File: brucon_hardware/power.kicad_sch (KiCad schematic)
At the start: 21 parts, among them J201 WTB01W03BB, Q1 AO3400A, U1 IP5305, U203 HT75xx-1-SOT89

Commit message: Small changes
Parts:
- R1: LCSC C22977 -> C270630
- R2: LCSC C25804 -> C25744
- R203, R204: LCSC C21189 -> C17168
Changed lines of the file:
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@@
 			)
 		)
-		(property "LCSC" "C21189"
+		(property "LCSC" " C17168"
 			(at 83.82 74.93 0)
 			(effects
@@
 			)
 		)
-		(property "LCSC" "C22977"
+		(property "LCSC" "C270630"
 			(at 52.07 69.85 0)
 			(effects
@@
 			)
 		)
-		(property "LCSC" "C25804"
+		(property "LCSC" "C25744"
 			(at 111.76 91.44 0)
 			(effects
@@
 			)
 		)
-		(property "LCSC" "C21189"
+		(property "LCSC" " C17168"
 			(at 76.2 69.85 0)
 			(effects

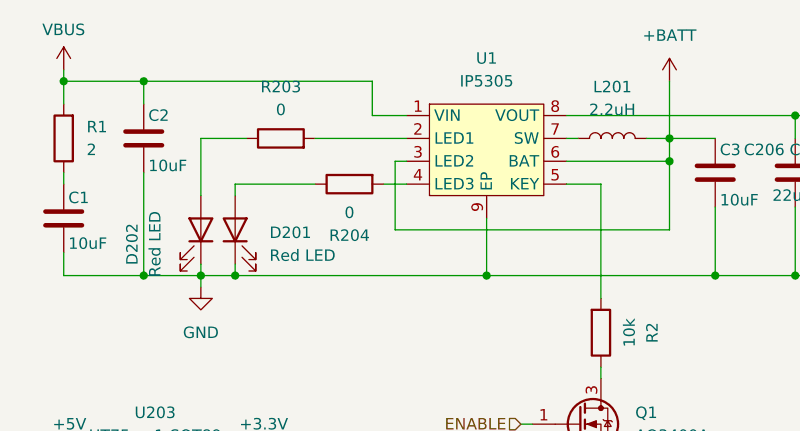
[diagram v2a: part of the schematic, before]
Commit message: Swapped IP5305 for IP5305T (needs current limiting resistors on LEDs), swapped buffer for Nexperia alternative for availability and price. Ordered 2nd prototype.
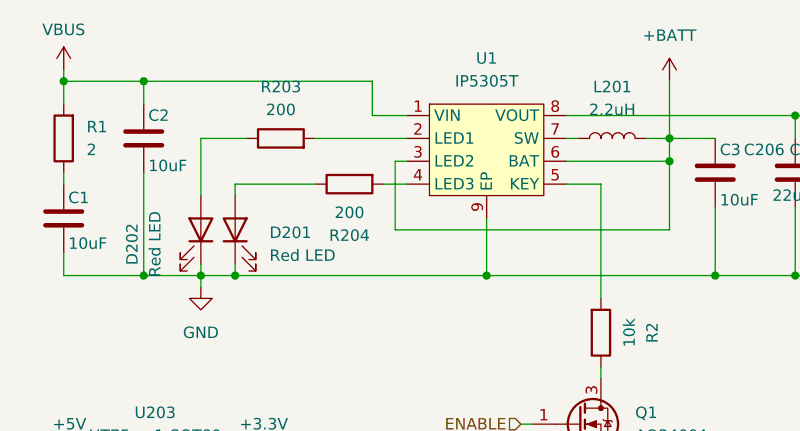
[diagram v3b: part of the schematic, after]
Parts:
- R203, R204: value 0 -> 200; LCSC C17168 -> C25087
- U1: value IP5305 -> IP5305T; LCSC C181686 -> C2982924
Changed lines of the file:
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@@
 			)
 		)
-		(property "Value" "0"
+		(property "Value" "200"
 			(at 83.82 78.105 90)
 			(effects
@@
 			)
 		)
-		(property "LCSC" " C17168"
+		(property "LCSC" "C25087"
 			(at 83.82 74.93 0)
 			(effects
@@
 			)
 		)
-		(property "Value" "IP5305"
+		(property "Value" "IP5305T"
 			(at 99.06 63.5 0)
 			(effects
@@
 			)
 		)
-		(property "Datasheet" "https://www.lcsc.com/datasheet/lcsc_datasheet_1810151710_INJOINIC-IP5305_C181686.pdf"
+		(property "Datasheet" "https://www.lcsc.com/datasheet/lcsc_datasheet_2311011131_INJOINIC-IP5305T_C2982924.pdf"
 			(at 96.52 68.58 0)
 			(effects
@@
 			)
 		)
-		(property "LCSC" "C181686"
+		(property "LCSC" "C2982924"
 			(at 99.06 69.85 0)
 			(effects
@@
 			)
 		)
-		(property "Value" "0"
+		(property "Value" "200"
 			(at 76.2 66.675 90)
 			(effects
@@
 			)
 		)
-		(property "LCSC" " C17168"
+		(property "LCSC" "C25087"
 			(at 76.2 69.85 0)
 			(effects

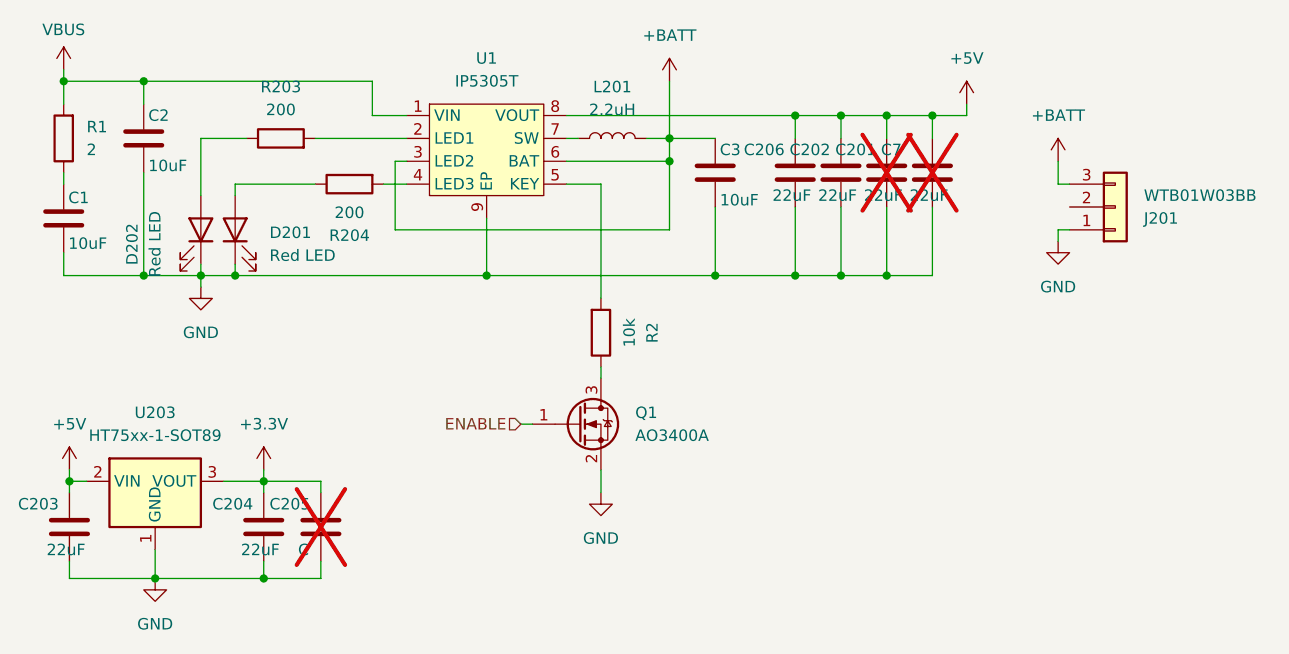
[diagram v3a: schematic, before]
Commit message: Committing final hardware as has been produced
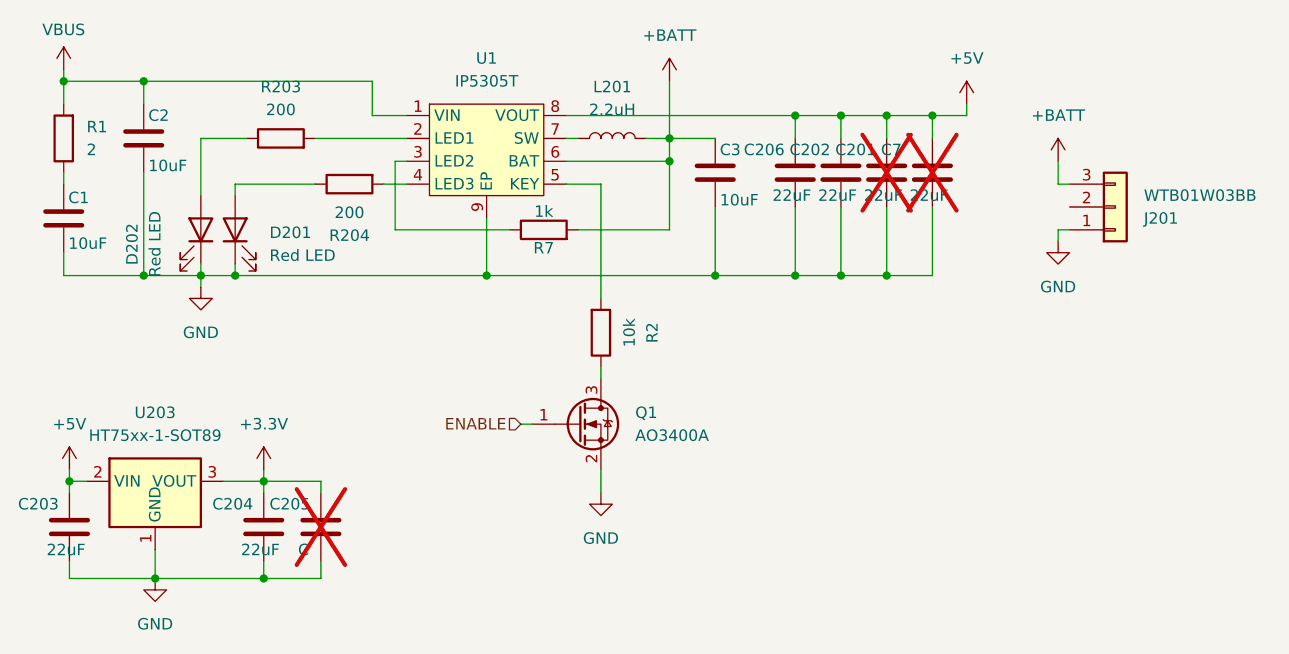
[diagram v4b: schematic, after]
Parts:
- added R7: 1k, Resistor_SMD:R_0402_1005Metric, symbol Device:R
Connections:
- net +BATT: now also R7.2; no longer U1.3 (LED2)
- new net: R7.1, U1.3 (LED2)
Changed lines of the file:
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@@
+	(wire
+		(pts
+			(xy 109.22 80.01) (xy 119.38 80.01)
+		)
+		(stroke
+			(width 0)
+			(type default)
+		)
+	)
 	(wire
 		(pts
@@
 	(wire
 		(pts
-			(xy 119.38 80.01) (xy 88.9 80.01)
-		)
-		(stroke
-			(width 0)
-			(type default)
-		)
-	)
-	(wire
-		(pts
 			(xy 52.705 118.745) (xy 62.23 118.745)
 		)
@@
 		(pts
 			(xy 80.01 74.93) (xy 71.12 74.93)
+		)
+		(stroke
+			(width 0)
+			(type default)
+		)
+	)
+	(wire
+		(pts
+			(xy 88.9 80.01) (xy 101.6 80.01)
 		)
 		(stroke
@@
 					(unit 1)
 				)
+			)
+		)
+	)
+	(symbol
+		(lib_id "Device:R")
+		(at 105.41 80.01 90)
+		(unit 1)
+		(exclude_from_sim no)
+		(in_bom yes)
+		(on_board yes)
+		(dnp no)
+		(property "Reference" "R7"
+			(at 105.41 82.042 90)
+			(effects
+				(font
+					(size 1.27 1.27)
+				)
+			)
+		)
+		(property "Value" "1k"
+			(at 105.41 77.978 90)
+			(effects
+				(font
+					(size 1.27 1.27)
+				)
+			)
+		)
+		(property "Footprint" "Resistor_SMD:R_0402_1005Metric"
+			(at 105.41 81.788 90)
+			(effects
+				(font
+					(size 1.27 1.27)
+				)
+				(hide yes)
+			)
+		)
+		(property "Datasheet" "~"
+			(at 105.41 80.01 0)
+			(effects
+				(font
+					(size 1.27 1.27)
+				)
+				(hide yes)
+			)
+		)
+		(property "Description" ""
+			(at 105.41 80.01 0)
+			(effects
+				(font
+					(size 1.27 1.27)
+				)
+				(hide yes)
+			)
+		)
+		(property "LCSC" " C11702"
+			(at 105.41 80.01 0)
+			(effects
+				(font
+					(size 1.27 1.27)
+				)
+				(hide yes)
+			)
+		)
+		(pin "2"
+		)
+		(pin "1"
+		)
+		(instances
+			(project "brucon_hardware"
+				(path "/c7d57f87-d402-454a-9407-398e29f51491/ccaf17dc-cf4f-4544-8bb8-0d800add2a3f"
+					(reference "R7")
+					(unit 1)
+				)
